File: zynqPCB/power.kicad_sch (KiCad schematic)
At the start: 60 parts, among them CON1 AVR-JTAG-10, U10 SC189 - 3.3V, U11 TLV62080DSGx, U12 SC189 - 1.8V, U20A1 xc7z020clg484, U20I1 xc7z020clg484, U7 LM3880, U8 LM3880, U9 SC189 - 1.0V

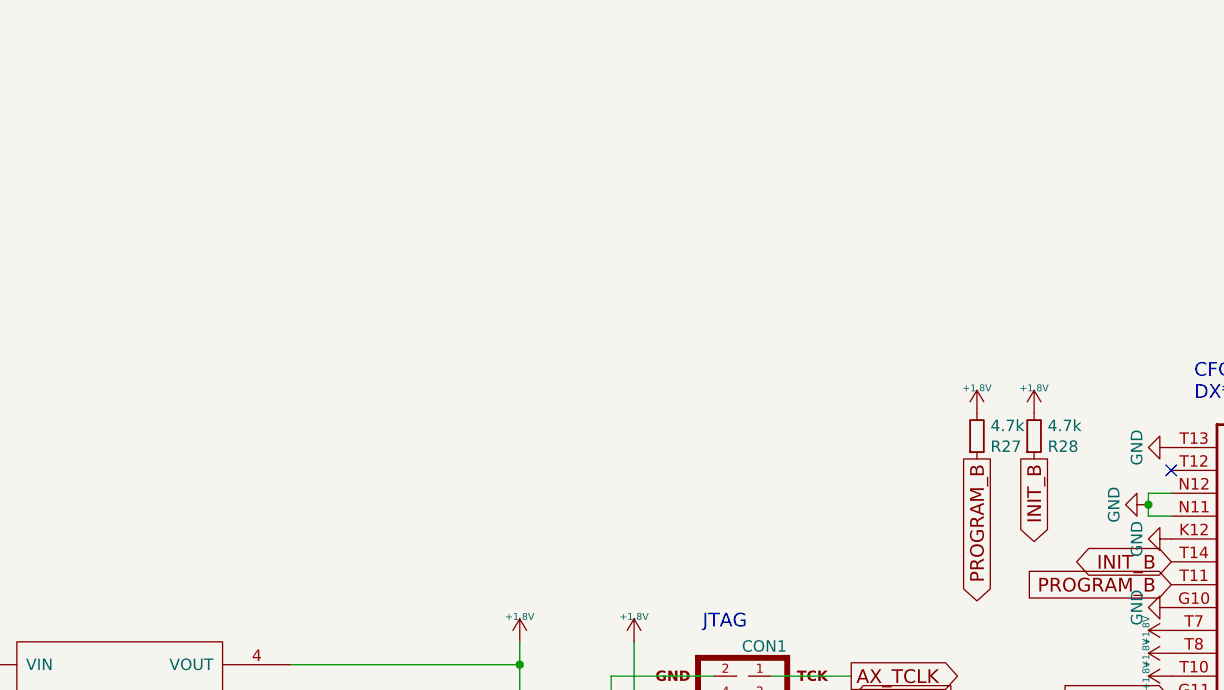
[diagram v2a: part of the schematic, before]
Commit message: USB-c power port
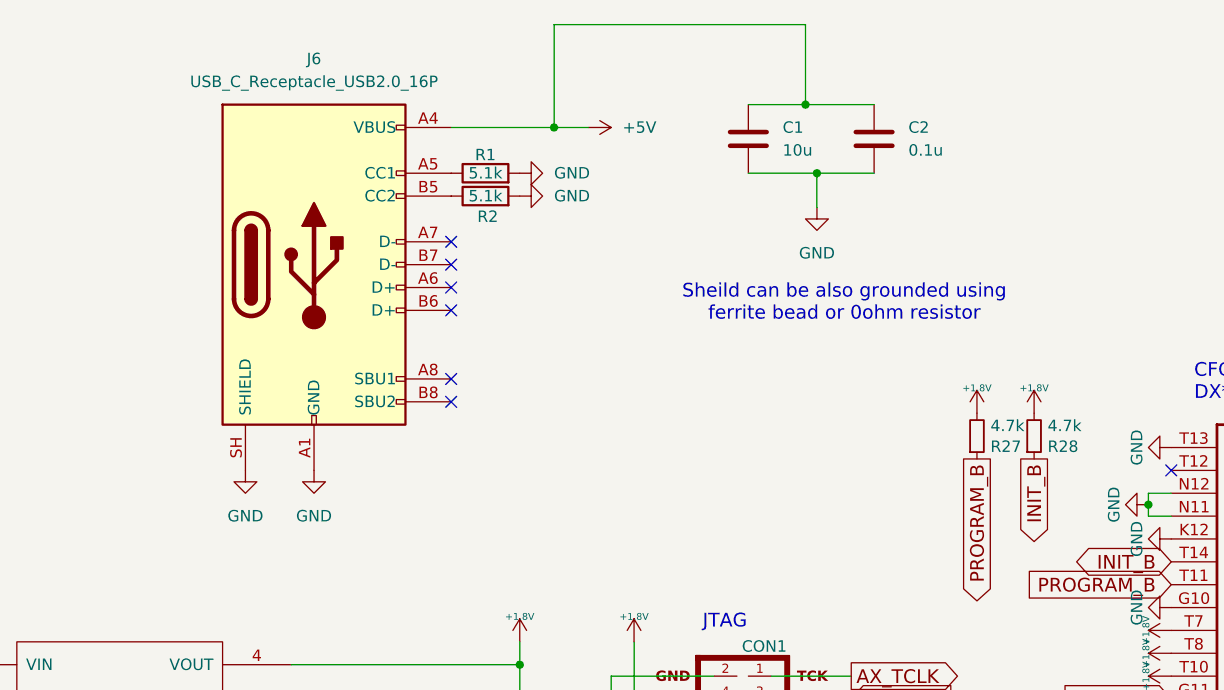
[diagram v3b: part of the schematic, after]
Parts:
- added C1: 10u, symbol Device:C
- added C2: 0.1u, symbol Device:C
- added J6: USB_C_Receptacle_USB2.0_16P, symbol Connector:USB_C_Receptacle_USB2.0_16P
- added R1, R2: 5.1k, symbol Device:R
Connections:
- net +5V: now also C1.1, C2.1, J6.A4 (VBUS), J6.A9 (VBUS), J6.B4 (VBUS), J6.B9 (VBUS)
- net GND: now also C1.2, C2.2, J6.A1 (GND), J6.A12 (GND), J6.B1 (GND), J6.B12 (GND), J6.SH (SHIELD), R1.2, R2.2
- new net: J6.B5 (CC2), R2.1
- new net: J6.A5 (CC1), R1.1
- no-connect marks 4 -> 10
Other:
- note added: "Sheild can be also grounded using ferrite bead or 0ohm resistor"

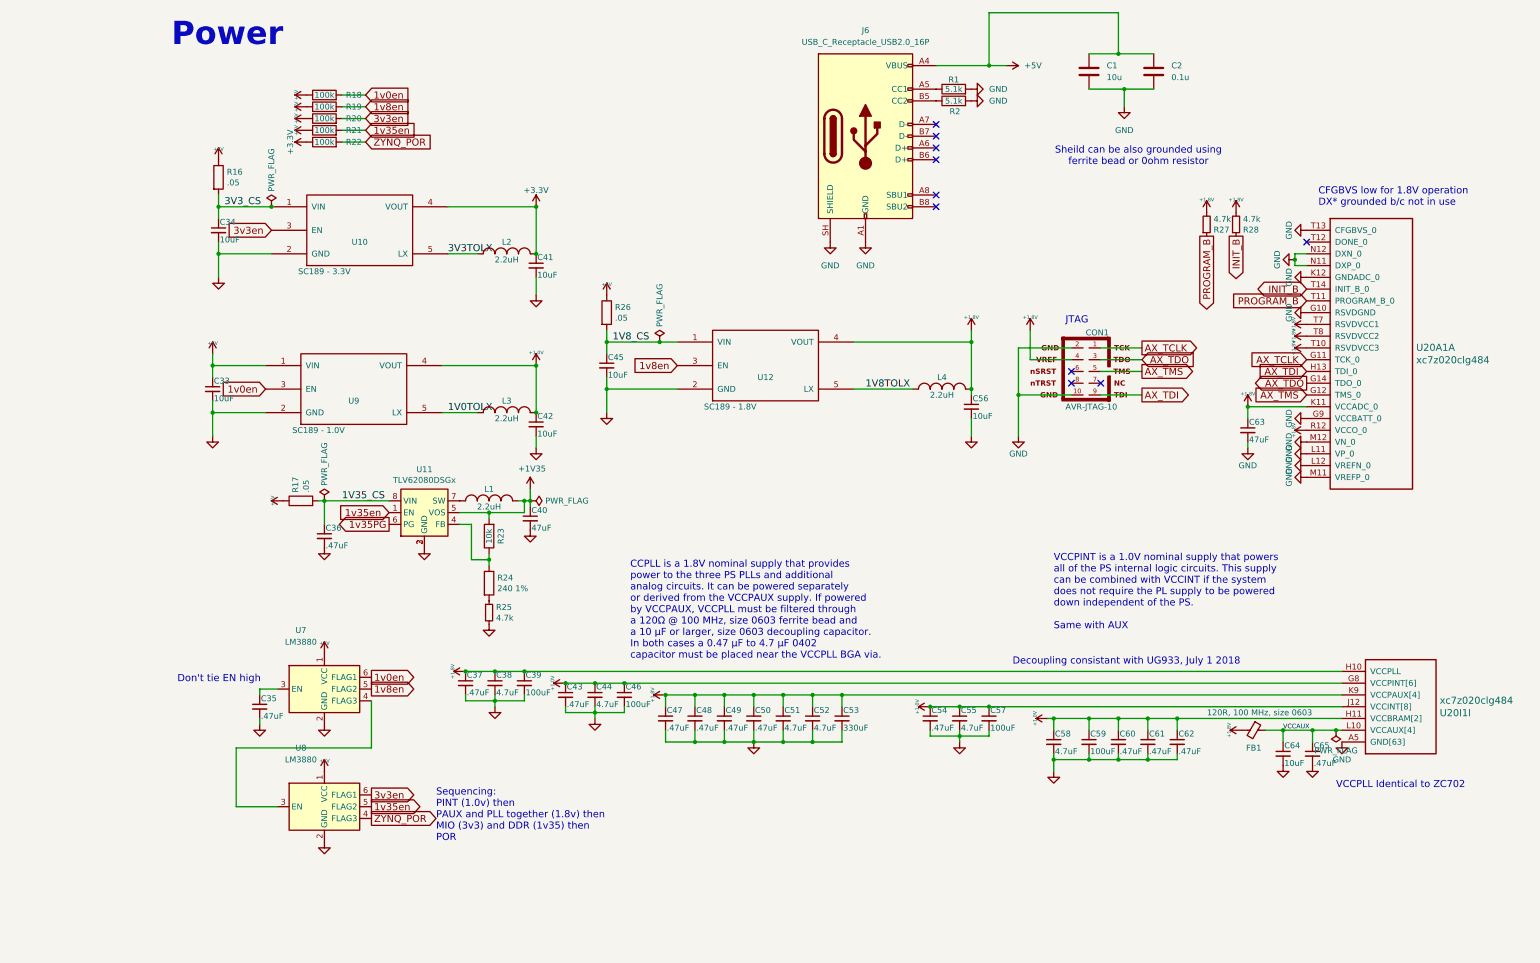
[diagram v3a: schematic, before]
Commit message: Cleared ERC error except the sequencer Part
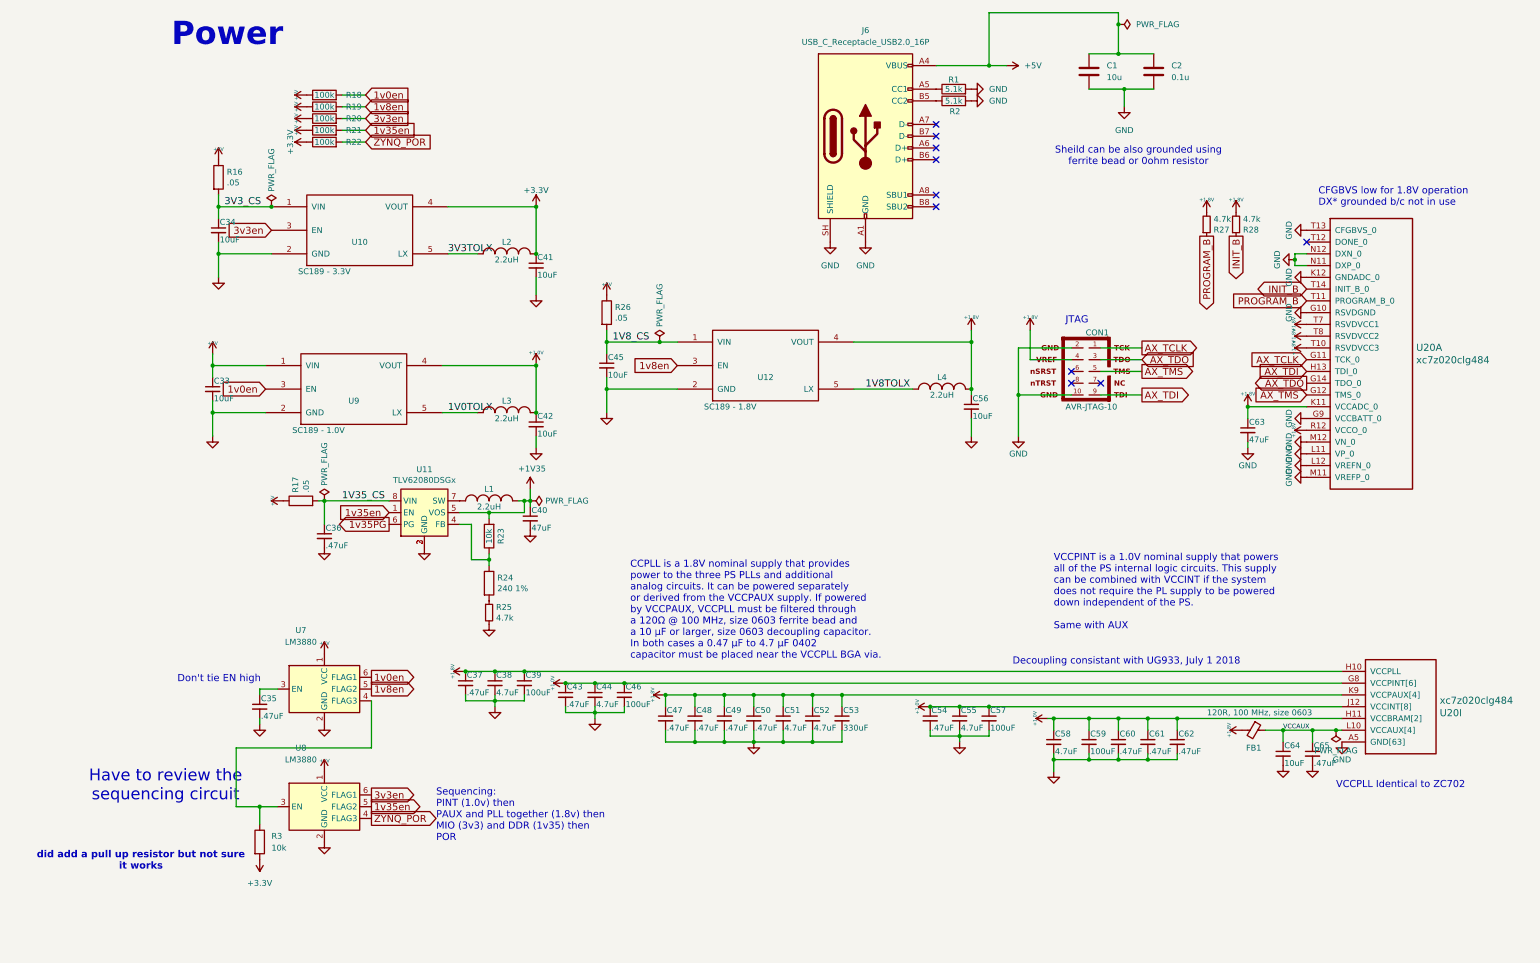
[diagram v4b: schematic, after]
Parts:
- added R3: 10k, symbol Device:R
- renumbered U20A1 to U20, U20I1 to U20
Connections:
- net +3.3V: now also R3.2
- net at U7.4 (FLAG3), U8.3 (EN): now also R3.1
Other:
- note added: "Have to review the sequencing circuit"
- note added: "did add a pull up resistor but not sure it works"

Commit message: Sequencing is taken care
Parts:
- removed C35: .47uF, Capacitor_SMD:C_0402_1005Metric, symbol Device:C_Small
- removed R3: 10k, symbol Device:R
- added FB2: 120R, 100 MHz, size 0603, Capacitor_SMD:C_0603_1608Metric, symbol Device:Ferrite_Bead_Small
- added U2: SN74AUP1G32DPWR, DPW0005A_TEX, symbol or gate:SN74AUP1G32DPWR
- added U3: SN74LVC1G08DSFR, SN74LVC1G08DSFR:SON35P100X100X40-6N, symbol Single and gate:SN74LVC1G08DSFR
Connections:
- net +5V: now also U2.1 (B), U2.5 (VCC), U3.1 (A), U3.6 (VCC)
- net 1v35en: now also U8.6 (FLAG1), U2.2 (A); no longer U8.5 (FLAG2)
- net 3v3en: now also U7.4 (FLAG3), U3.2 (B); no longer U8.6 (FLAG1)
- net GND: now also FB2.1, U2.3 (GND), U3.3 (GND); no longer J6.SH (SHIELD)
- net ZYNQ_POR: now also U8.5 (FLAG2); no longer U8.4 (FLAG3)
- net at U7.3 (EN): now also U2.4 (Y)
- net at U8.3 (EN): now also U3.4 (Y); no longer U7.4 (FLAG3)
- new net: FB2.2, J6.SH (SHIELD)
- no-connect marks 10 -> 12
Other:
- note added: "Power flag to indicate just only clear the ERC"
- note removed: "Have to review the sequencing circuit"
- note removed: "did add a pull up resistor but not sure it works"
- moved on the sheet: U7, U8

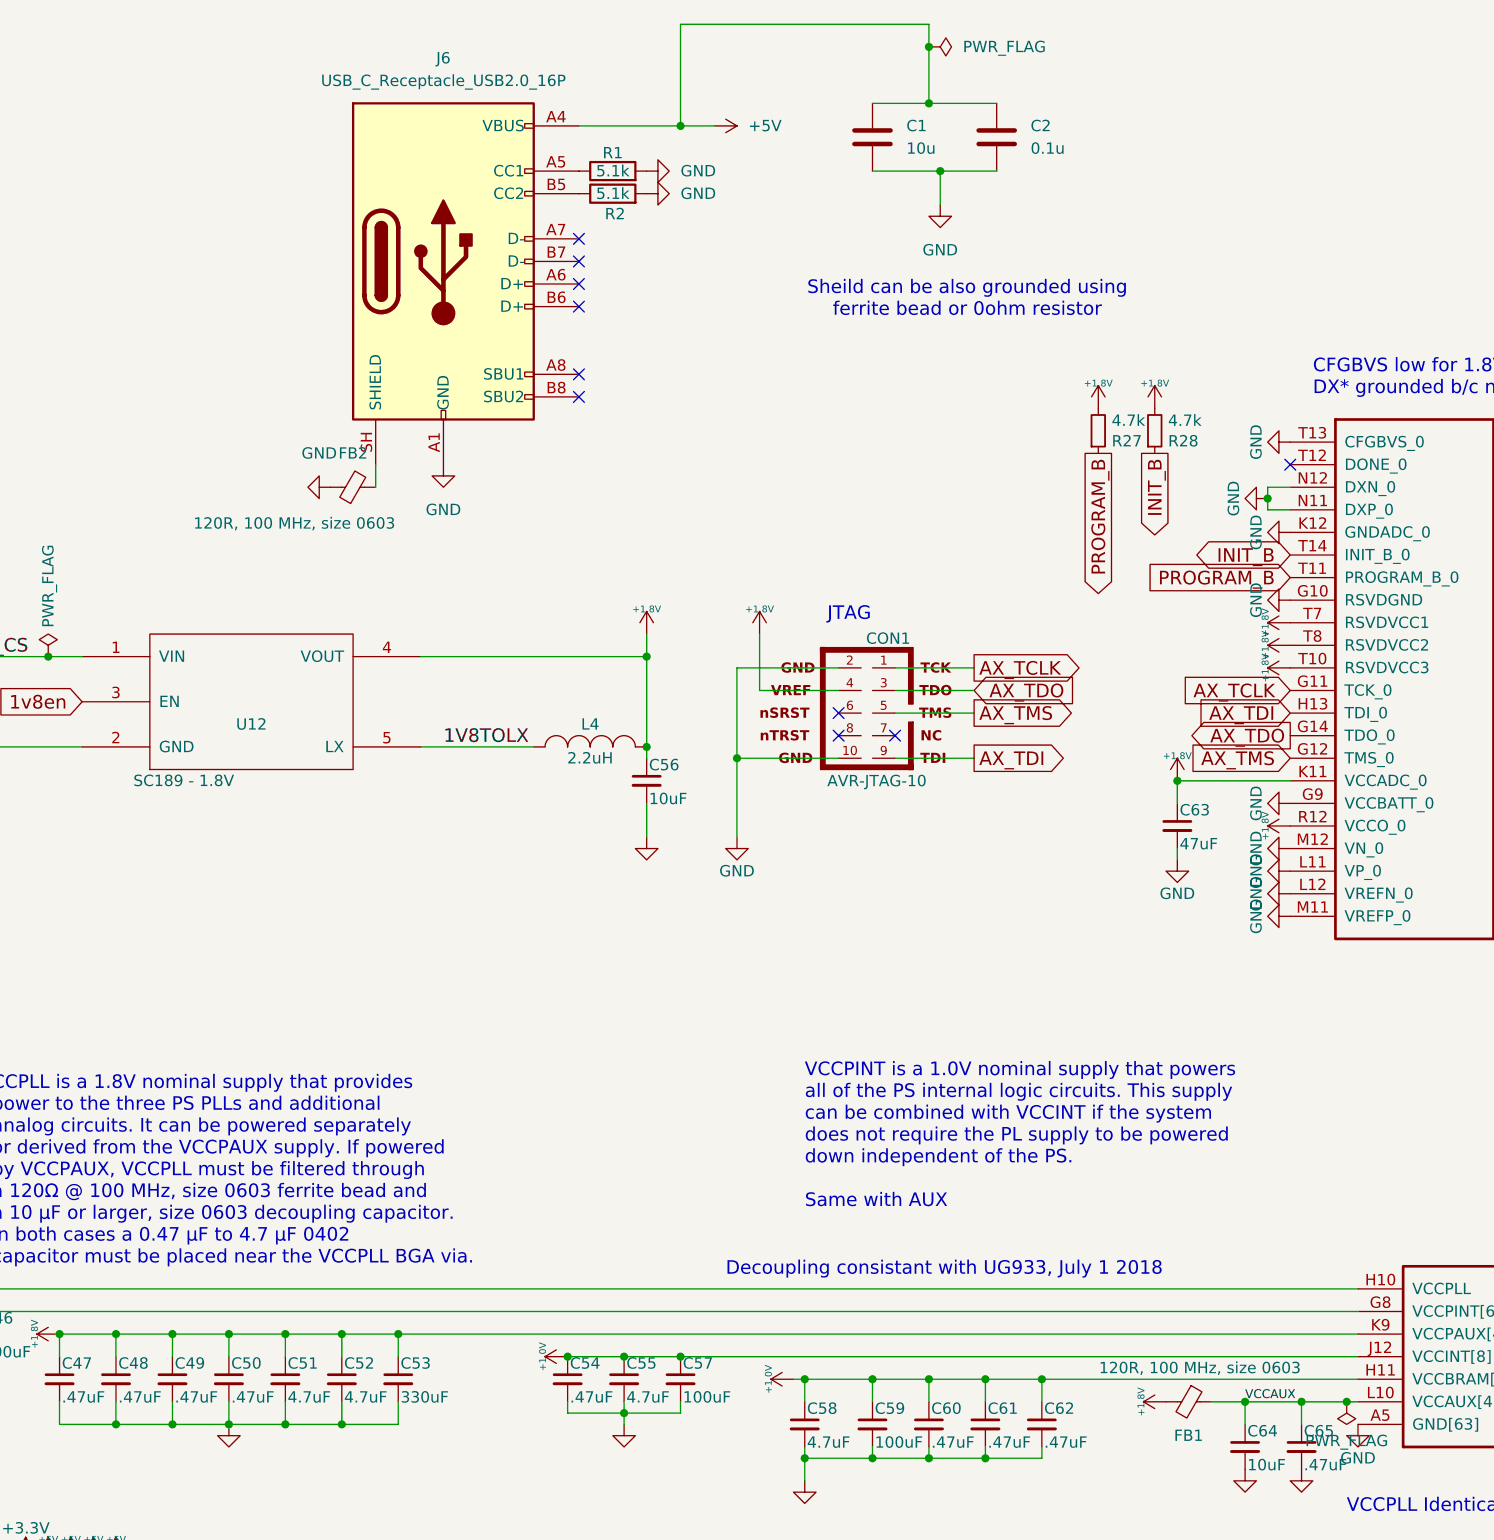
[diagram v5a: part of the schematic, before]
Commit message: Sanity Checks and added some footprints
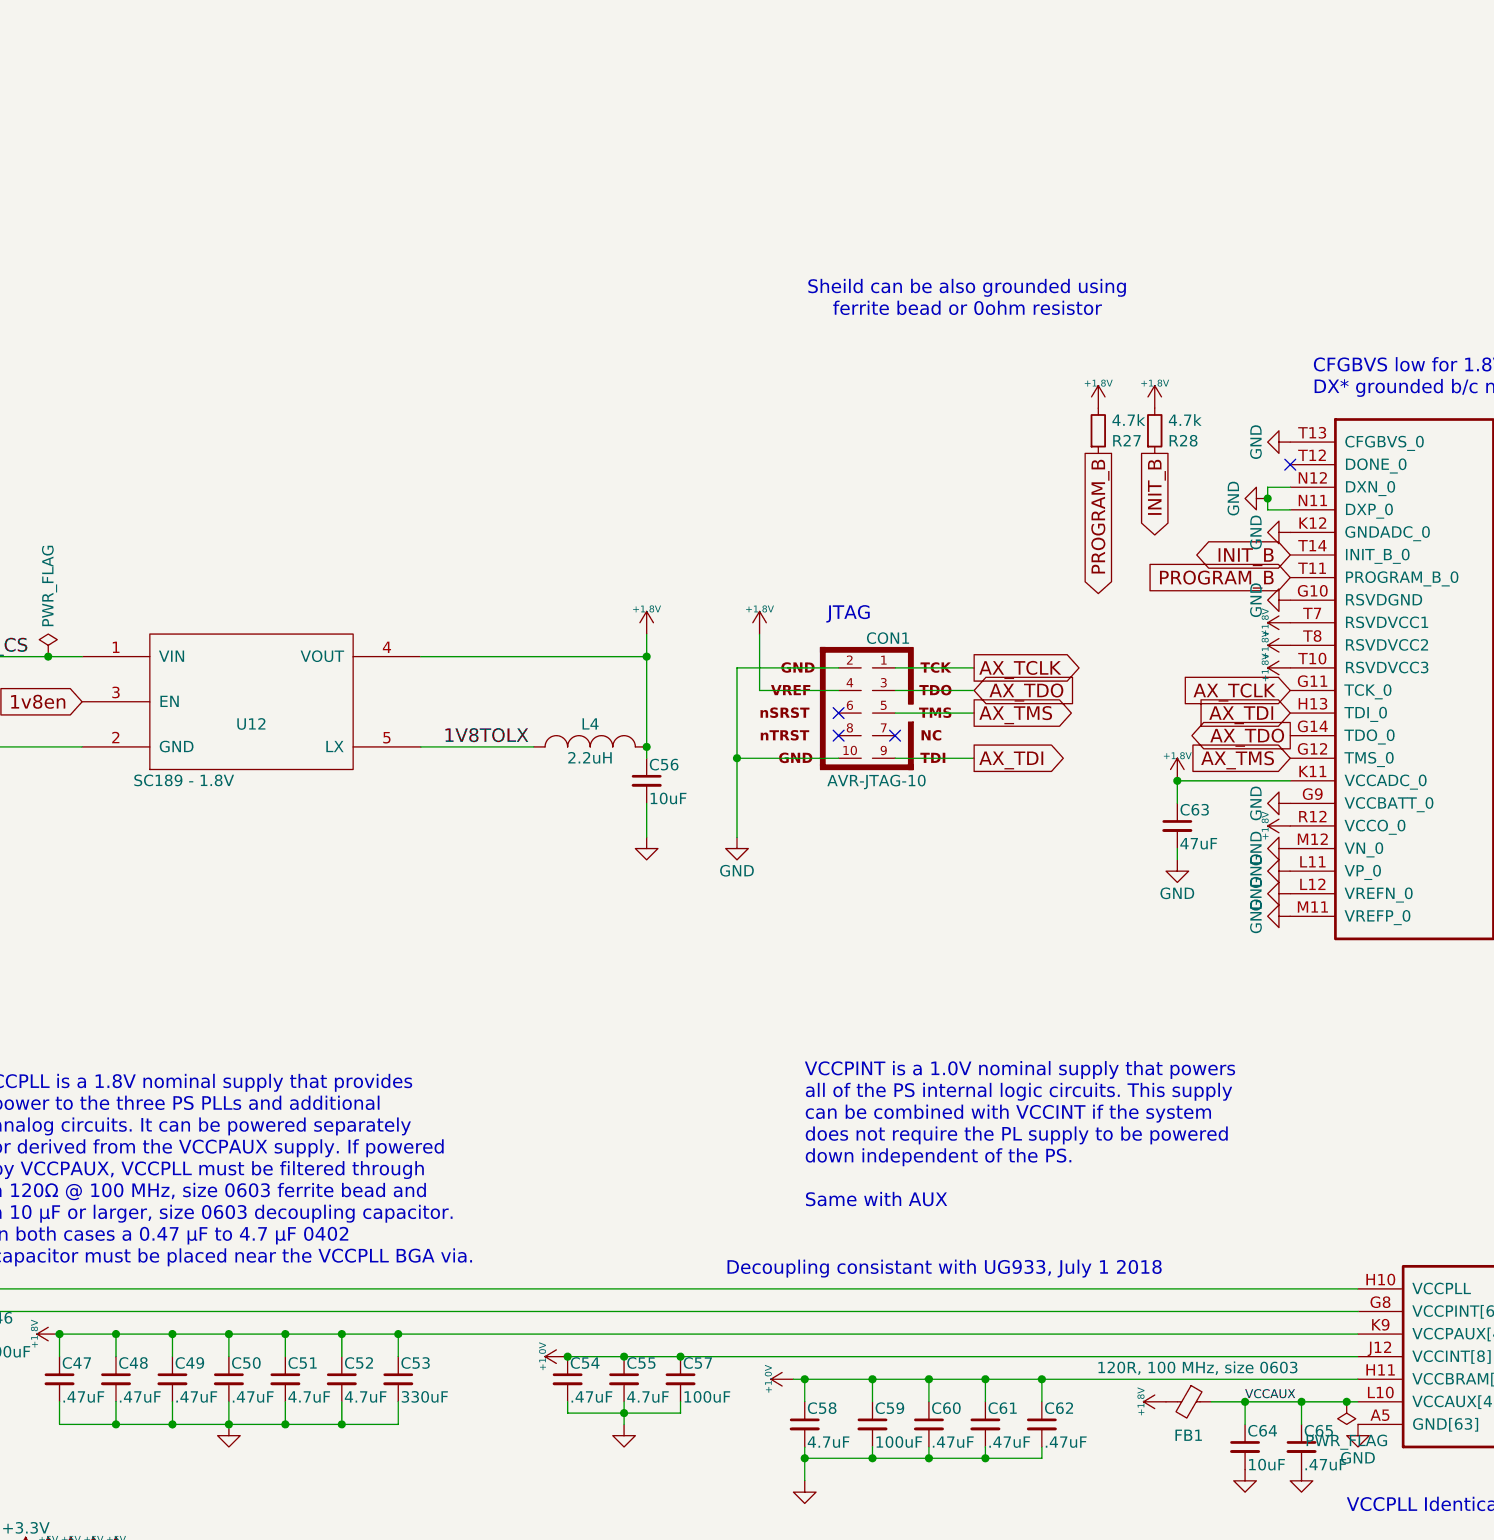
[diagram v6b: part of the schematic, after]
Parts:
- removed C1: 10u, symbol Device:C
- removed C2: 0.1u, symbol Device:C
- removed FB2: 120R, 100 MHz, size 0603, Capacitor_SMD:C_0603_1608Metric, symbol Device:Ferrite_Bead_Small
- removed J6: USB_C_Receptacle_USB2.0_16P, symbol Connector:USB_C_Receptacle_USB2.0_16P
- removed R1, R2: 5.1k, symbol Device:R
- FB1: footprint Capacitor_SMD:C_0603_1608Metric -> Inductor_SMD:L_0603_1608Metric
- U2: footprint DPW0005A_TEX -> Or_gate:DPW0005A_TEX
- U3: footprint SN74LVC1G08DSFR:SON35P100X100X40-6N -> SINGLE_AND_GATE:SON35P100X100X40-6N
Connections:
- no-connect marks 12 -> 6
